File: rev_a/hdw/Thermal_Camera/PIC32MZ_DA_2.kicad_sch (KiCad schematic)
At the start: 1 part

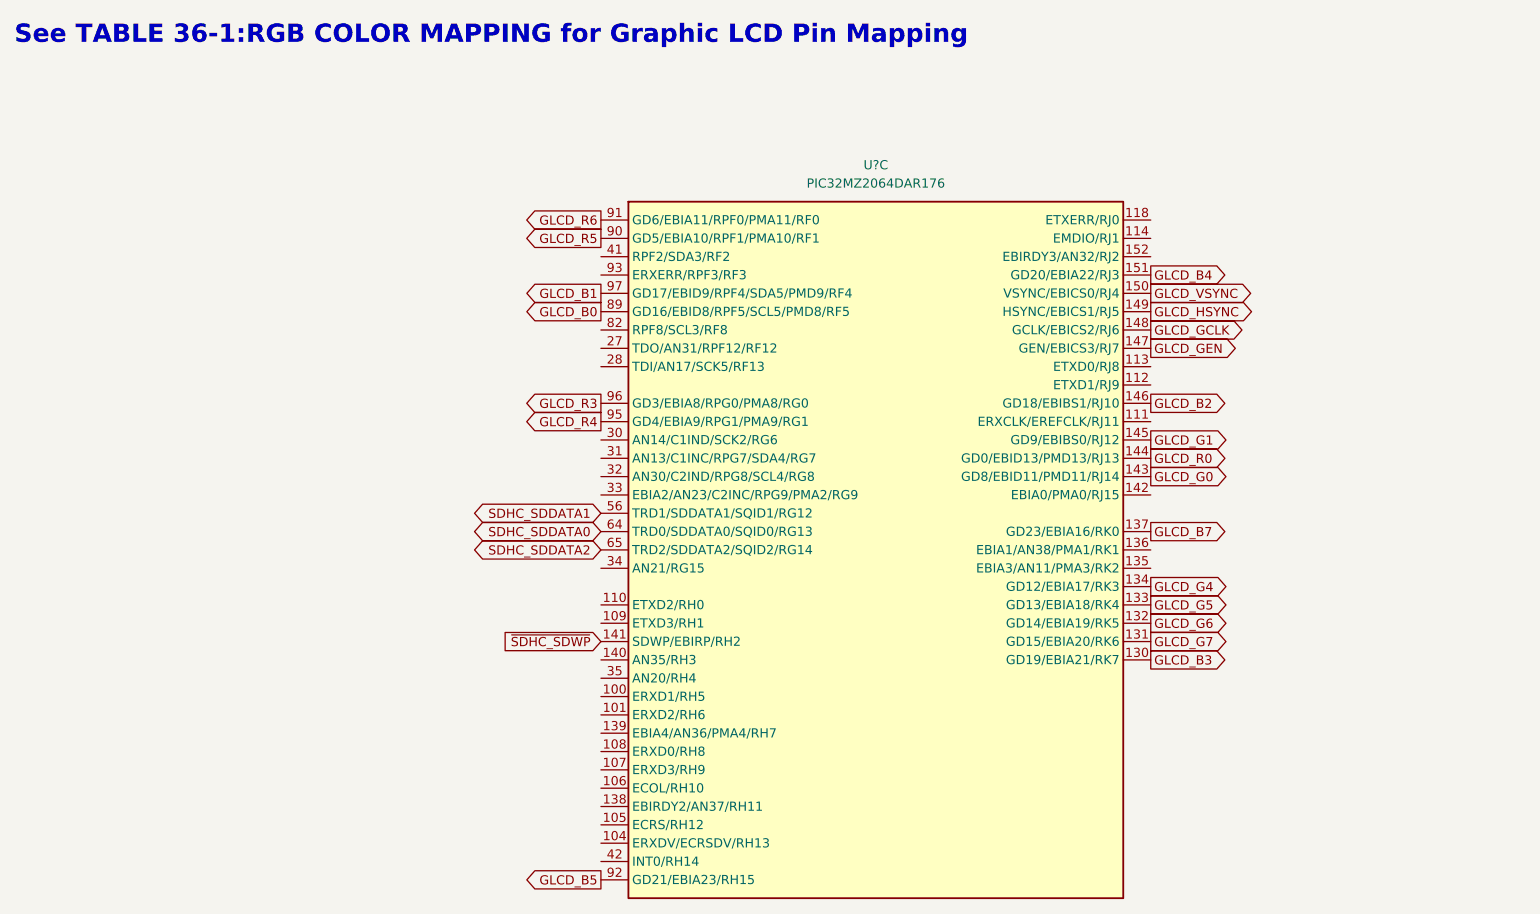
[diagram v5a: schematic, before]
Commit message: assigned some GPIO pins
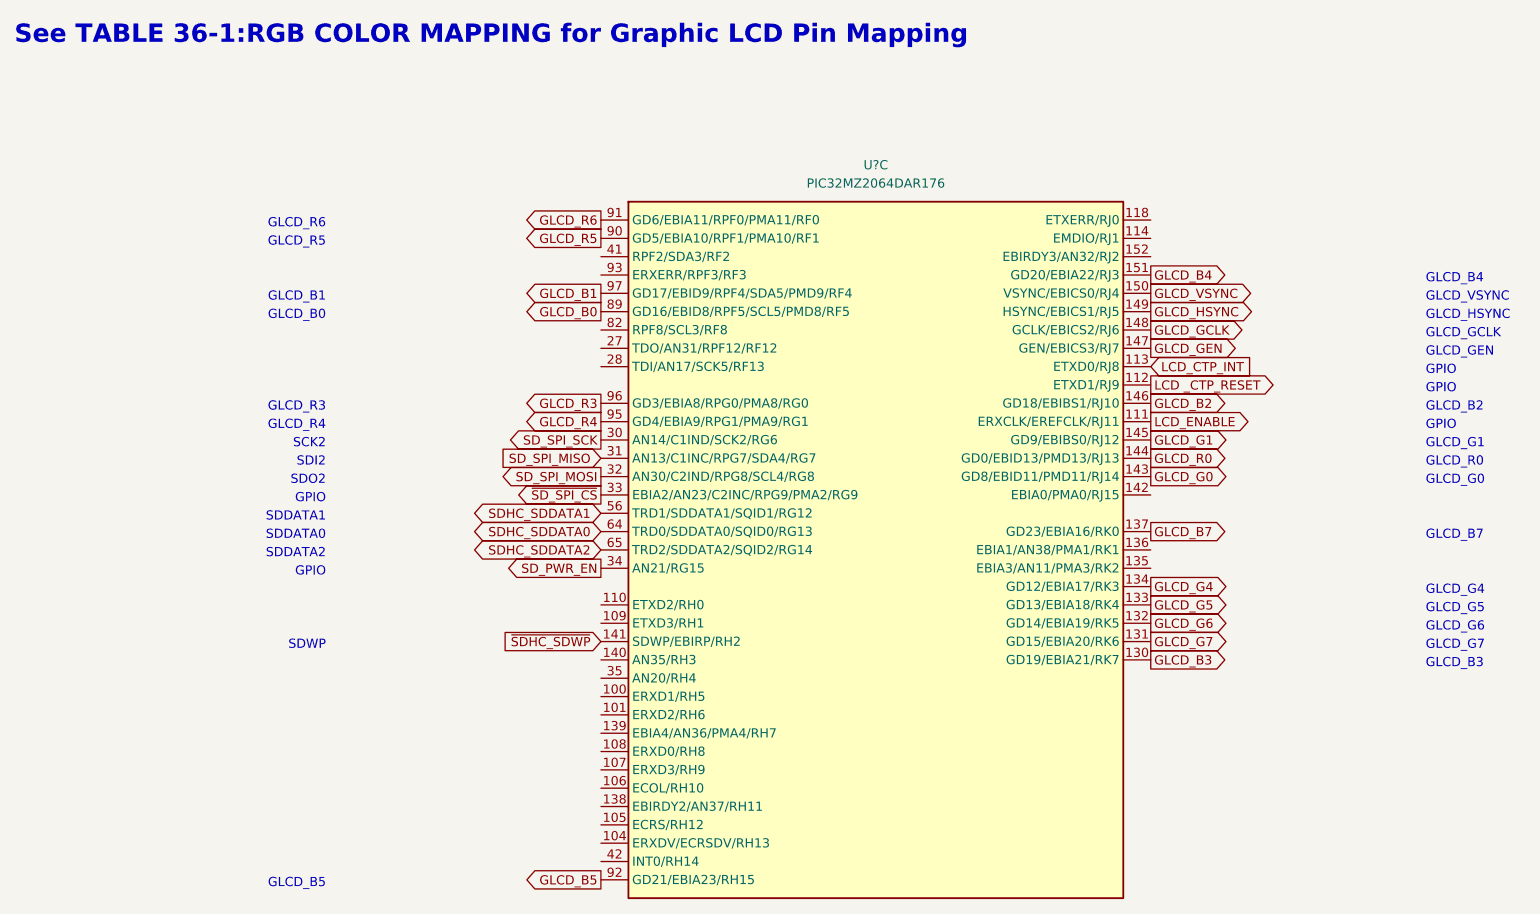
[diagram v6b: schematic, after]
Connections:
- net LCD_ENABLE: now reaches U?.111 (ERXCLK/EREFCLK/RJ11)
- net LCD _CTP_RESET: now reaches U?.112 (ETXD1/RJ9)
- net LCD_CTP_INT: now reaches U?.113 (ETXD0/RJ8)
- net SD_SPI_SCK: now reaches U?.30 (AN14/C1IND/SCK2/RG6)
- net SD_SPI_MISO: now reaches U?.31 (AN13/C1INC/RPG7/SDA4/RG7)
- net SD_SPI_MOSI: now reaches U?.32 (AN30/C2IND/RPG8/SCL4/RG8)
- net ~{SD_SPI_CS}: now reaches U?.33 (EBIA2/AN23/C2INC/RPG9/PMA2/RG9)
- net SD_PWR_EN: now reaches U?.34 (AN21/RG15)
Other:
- note added: "GLCD_B0"
- note added: "GLCD_B1"
- note added: "GLCD_B2"
- note added: "GLCD_B3"
- note added: "GLCD_B4"
- note added: "GLCD_B5"
- note added: "GLCD_B7"
- note added: "GLCD_G0"
- note added: "GLCD_G1"
- note added: "GLCD_G4"
- note added: "GLCD_G5"
- note added: "GLCD_G6"
- note added: "GLCD_G7"
- note added: "GLCD_GCLK"
- note added: "GLCD_GEN"
- note added: "GLCD_HSYNC"
- note added: "GLCD_R0"
- note added: "GLCD_R3"
- note added: "GLCD_R4"
- note added: "GLCD_R5"
- note added: "GLCD_R6"
- note added: "GLCD_VSYNC"
- note added: "GPIO"
- note added: "SCK2"
- note added: "SDDATA0"
- note added: "SDDATA1"
- note added: "SDDATA2"
- note added: "SDI2"
- note added: "SDO2"
- note added: "SDWP"
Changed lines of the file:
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@@
     (company "Drew Maatman and Michael Laffin")
+  )
+  (text "GLCD_G7" (at 210.82 101.6 0)
+    (effects (font (size 1.27 1.27)) (justify left bottom))
+  )
+  (text "GPIO" (at 210.82 63.5 0)
+    (effects (font (size 1.27 1.27)) (justify left bottom))
+  )
+  (text "GLCD_GEN" (at 210.82 60.96 0)
+    (effects (font (size 1.27 1.27)) (justify left bottom))
+  )
+  (text "GLCD_VSYNC" (at 210.82 53.34 0)
+    (effects (font (size 1.27 1.27)) (justify left bottom))
+  )
+  (text "GLCD_B0" (at 58.42 55.88 0)
+    (effects (font (size 1.27 1.27)) (justify right bottom))
+  )
+  (text "GLCD_R6" (at 58.42 43.18 0)
+    (effects (font (size 1.27 1.27)) (justify right bottom))
+  )
+  (text "GLCD_G0\n" (at 210.82 78.74 0)
+    (effects (font (size 1.27 1.27)) (justify left bottom))
+  )
+  (text "SDDATA0" (at 58.42 86.36 0)
+    (effects (font (size 1.27 1.27)) (justify right bottom))
+  )
+  (text "GLCD_HSYNC" (at 210.82 55.88 0)
+    (effects (font (size 1.27 1.27)) (justify left bottom))
+  )
+  (text "GPIO" (at 210.82 71.12 0)
+    (effects (font (size 1.27 1.27)) (justify left bottom))
+  )
+  (text "GPIO" (at 210.82 66.04 0)
+    (effects (font (size 1.27 1.27)) (justify left bottom))
+  )
+  (text "GLCD_B4" (at 210.82 50.8 0)
+    (effects (font (size 1.27 1.27)) (justify left bottom))
+  )
+  (text "GPIO" (at 58.42 81.28 0)
+    (effects (font (size 1.27 1.27)) (justify right bottom))
+  )
+  (text "GLCD_GCLK" (at 210.82 58.42 0)
+    (effects (font (size 1.27 1.27)) (justify left bottom))
+  )
+  (text "GLCD_G6" (at 210.82 99.06 0)
+    (effects (font (size 1.27 1.27)) (justify left bottom))
+  )
+  (text "SDDATA2" (at 58.42 88.9 0)
+    (effects (font (size 1.27 1.27)) (justify right bottom))
+  )
+  (text "GLCD_B5" (at 58.42 134.62 0)
+    (effects (font (size 1.27 1.27)) (justify right bottom))
+  )
+  (text "GLCD_R0\n" (at 210.82 76.2 0)
+    (effects (font (size 1.27 1.27)) (justify left bottom))
+  )
+  (text "GLCD_B1" (at 58.42 53.34 0)
+    (effects (font (size 1.27 1.27)) (justify right bottom))
+  )
+  (text "SDI2" (at 58.42 76.2 0)
+    (effects (font (size 1.27 1.27)) (justify right bottom))
+  )
+  (text "GLCD_G4\n" (at 210.82 93.98 0)
+    (effects (font (size 1.27 1.27)) (justify left bottom))
+  )
+  (text "GLCD_R3" (at 58.42 68.58 0)
+    (effects (font (size 1.27 1.27)) (justify right bottom))
+  )
+  (text "GLCD_R4" (at 58.42 71.12 0)
+    (effects (font (size 1.27 1.27)) (justify right bottom))
+  )
+  (text "SCK2" (at 58.42 73.66 0)
+    (effects (font (size 1.27 1.27)) (justify right bottom))
+  )
+  (text "SDWP" (at 58.42 101.6 0)
+    (effects (font (size 1.27 1.27)) (justify right bottom))
   )
   (text "See TABLE 36-1:RGB COLOR MAPPING for Graphic LCD Pin Mapping"
@@
     (effects (font (face "Courier New") (size 2.54 2.54) (thickness 0.254) bold) (justify left bottom))
   )
+  (text "SDDATA1" (at 58.42 83.82 0)
+    (effects (font (size 1.27 1.27)) (justify right bottom))
+  )
+  (text "GLCD_G5" (at 210.82 96.52 0)
+    (effects (font (size 1.27 1.27)) (justify left bottom))
+  )
+  (text "SDO2" (at 58.42 78.74 0)
+    (effects (font (size 1.27 1.27)) (justify right bottom))
+  )
+  (text "GLCD_R5" (at 58.42 45.72 0)
+    (effects (font (size 1.27 1.27)) (justify right bottom))
+  )
+  (text "GLCD_B7\n" (at 210.82 86.36 0)
+    (effects (font (size 1.27 1.27)) (justify left bottom))
+  )
+  (text "GLCD_B3" (at 210.82 104.14 0)
+    (effects (font (size 1.27 1.27)) (justify left bottom))
+  )
+  (text "GLCD_G1\n" (at 210.82 73.66 0)
+    (effects (font (size 1.27 1.27)) (justify left bottom))
+  )
+  (text "GLCD_B2" (at 210.82 68.58 0)
+    (effects (font (size 1.27 1.27)) (justify left bottom))
+  )
+  (text "GPIO" (at 58.42 91.44 0)
+    (effects (font (size 1.27 1.27)) (justify right bottom))
+  )
   (global_label "GLCD_R4" (shape output) (at 96.52 69.85 180) (fields_autoplaced)
     (effects (font (size 1.27 1.27)) (justify right))
@@
     )
   )
+  (global_label "SD_SPI_MOSI" (shape output) (at 96.52 77.47 180) (fields_autoplaced)
+    (effects (font (size 1.27 1.27)) (justify right))
+    (property "Intersheetrefs" "${INTERSHEET_REFS}" (at 81.519 77.47 0)
+      (effects (font (size 1.27 1.27)) (justify right) hide)
+    )
+  )
   (global_label "GLCD_G1" (shape output) (at 172.72 72.39 0) (fields_autoplaced)
     (effects (font (size 1.27 1.27)) (justify left))
@@
     )
   )
+  (global_label "LCD _CTP_RESET" (shape output) (at 172.72 64.77 0) (fields_autoplaced)
+    (effects (font (size 1.27 1.27)) (justify left))
+    (property "Intersheetrefs" "${INTERSHEET_REFS}" (at 191.3494 64.77 0)
+      (effects (font (size 1.27 1.27)) (justify left) hide)
+    )
+  )
   (global_label "GLCD_B7" (shape output) (at 172.72 85.09 0) (fields_autoplaced)
     (effects (font (size 1.27 1.27)) (justify left))
@@
     )
   )
+  (global_label "SD_SPI_SCK" (shape output) (at 96.52 72.39 180) (fields_autoplaced)
+    (effects (font (size 1.27 1.27)) (justify right))
+    (property "Intersheetrefs" "${INTERSHEET_REFS}" (at 82.3657 72.39 0)
+      (effects (font (size 1.27 1.27)) (justify right) hide)
+    )
+  )
   (global_label "GLCD_G4" (shape output) (at 172.72 92.71 0) (fields_autoplaced)
     (effects (font (size 1.27 1.27)) (justify left))
@@
     )
   )
+  (global_label "SD_PWR_EN" (shape output) (at 96.52 90.17 180) (fields_autoplaced)
+    (effects (font (size 1.27 1.27)) (justify right))
+    (property "Intersheetrefs" "${INTERSHEET_REFS}" (at 82.7286 90.17 0)
+      (effects (font (size 1.27 1.27)) (justify right) hide)
+    )
+  )
   (global_label "SDHC_SDDATA0" (shape bidirectional) (at 96.52 85.09 180) (fields_autoplaced)
     (effects (font (size 1.27 1.27)) (justify right))
@@
     )
   )
+  (global_label "SD_SPI_MISO" (shape input) (at 96.52 74.93 180) (fields_autoplaced)
+    (effects (font (size 1.27 1.27)) (justify right))
+    (property "Intersheetrefs" "${INTERSHEET_REFS}" (at 81.519 74.93 0)
+      (effects (font (size 1.27 1.27)) (justify right) hide)
+    )
+  )
   (global_label "GLCD_B4" (shape output) (at 172.72 49.53 0) (fields_autoplaced)
     (effects (font (size 1.27 1.27)) (justify left))
@@
     )
   )
+  (global_label "LCD_CTP_INT" (shape input) (at 172.72 62.23 0) (fields_autoplaced)
+    (effects (font (size 1.27 1.27)) (justify left))
+    (property "Intersheetrefs" "${INTERSHEET_REFS}" (at 187.5396 62.23 0)
+      (effects (font (size 1.27 1.27)) (justify left) hide)
+    )
+  )
+  (global_label "LCD_ENABLE" (shape output) (at 172.72 69.85 0) (fields_autoplaced)
+    (effects (font (size 1.27 1.27)) (justify left))
+    (property "Intersheetrefs" "${INTERSHEET_REFS}" (at 187.1767 69.85 0)
+      (effects (font (size 1.27 1.27)) (justify left) hide)
+    )
+  )
+  (global_label "~{SD_SPI_CS}" (shape output) (at 96.52 80.01 180) (fields_autoplaced)
+    (effects (font (size 1.27 1.27)) (justify right))
+    (property "Intersheetrefs" "${INTERSHEET_REFS}" (at 83.6357 80.01 0)
+      (effects (font (size 1.27 1.27)) (justify right) hide)
+    )
+  )

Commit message: blah blah
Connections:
- net POS12_PGOOD: now reaches U?.100 (ERXD1/RH5)
- net POS3P0_PGOOD: now reaches U?.101 (ERXD2/RH6)
- net POS1P2_RUN: now reaches U?.104 (ERXDV/ECRSDV/RH13)
- net POS1P2_PGOOD: now reaches U?.105 (ECRS/RH12)
- net PGOOD_LED_SHDN: now reaches U?.106 (ECOL/RH10)
- net POS2P8_RUN: now reaches U?.107 (ERXD3/RH9)
- net POS2P8_PGOOD: now reaches U?.108 (ERXD0/RH8)
- net POS1P8_PGOOD: now reaches U?.139 (EBIA4/AN36/PMA4/RH7)

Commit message: lots of schematic progress
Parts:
- gave numbers to parts that had none: 1
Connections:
- no-connect marks 0 -> 17
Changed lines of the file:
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@@
 	(title_block
 		(title "Thermal Camera")
-		(date "2023-12-07")
+		(date "2024-05-24")
 		(rev "PRELIM")
 		(company "Drew Maatman and Michael Laffin")
+	)
+	(no_connect
+		(at 96.52 49.53)
+	)
+	(no_connect
+		(at 96.52 62.23)
+	)
+	(no_connect
+		(at 96.52 130.81)
+	)
+	(no_connect
+		(at 96.52 57.15)
+	)
+	(no_connect
+		(at 96.52 123.19)
+	)
+	(no_connect
+		(at 96.52 46.99)
+	)
+	(no_connect
+		(at 172.72 46.99)
+	)
+	(no_connect
+		(at 172.72 80.01)
+	)
+	(no_connect
+		(at 96.52 102.87)
+	)
+	(no_connect
+		(at 96.52 105.41)
+	)
+	(no_connect
+		(at 172.72 87.63)
+	)
+	(no_connect
+		(at 96.52 97.79)
+	)
+	(no_connect
+		(at 96.52 95.25)
+	)
+	(no_connect
+		(at 172.72 90.17)
+	)
+	(no_connect
+		(at 96.52 59.69)
+	)
+	(no_connect
+		(at 172.72 41.91)
+	)
+	(no_connect
+		(at 172.72 44.45)
 	)
 	(text "GLCD_G7"
@@
 		(dnp no)
 		(fields_autoplaced yes)
-		(property "Reference" "U?"
+		(property "Reference" "U1901"
 			(at 134.62 34.29 0)
 			(effects
@@
 			(project "Thermal_Camera"
 				(path "/4bd21e0b-5408-4b93-866e-c82ac5b31fa9/d6dd27c9-8e5b-4d17-a34a-73b51937c448"
-					(reference "U?")
+					(reference "U1901")
 					(unit 3)
 				)
